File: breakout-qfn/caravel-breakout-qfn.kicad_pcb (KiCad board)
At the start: 2 copper layers, 45 x 52.5 mm, 42 parts, among them CON1 REF-182665-01, CON2 REF-182665-01, CON3 73251-1352, U1 Caravel_QFN, U2 TLV73318PDBV

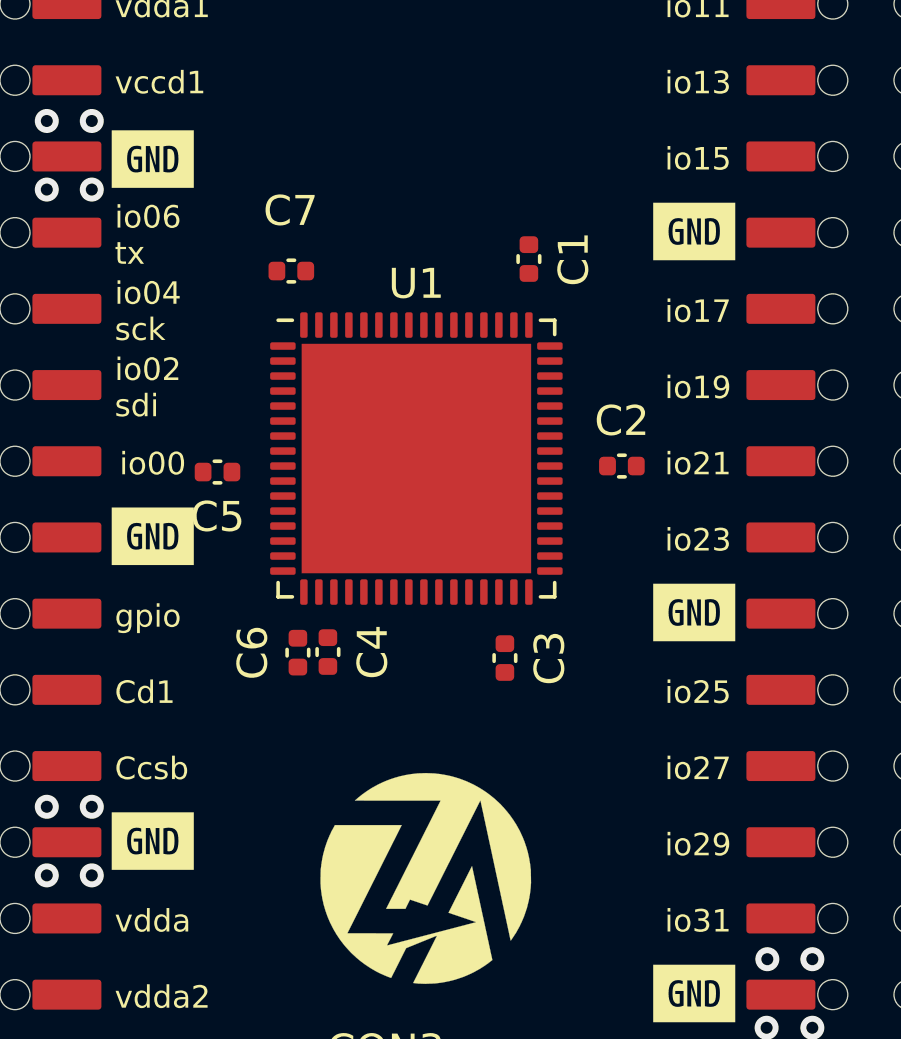
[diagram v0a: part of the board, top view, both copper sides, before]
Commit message: pre-route, DRC setup, floorplan for 2-layer top
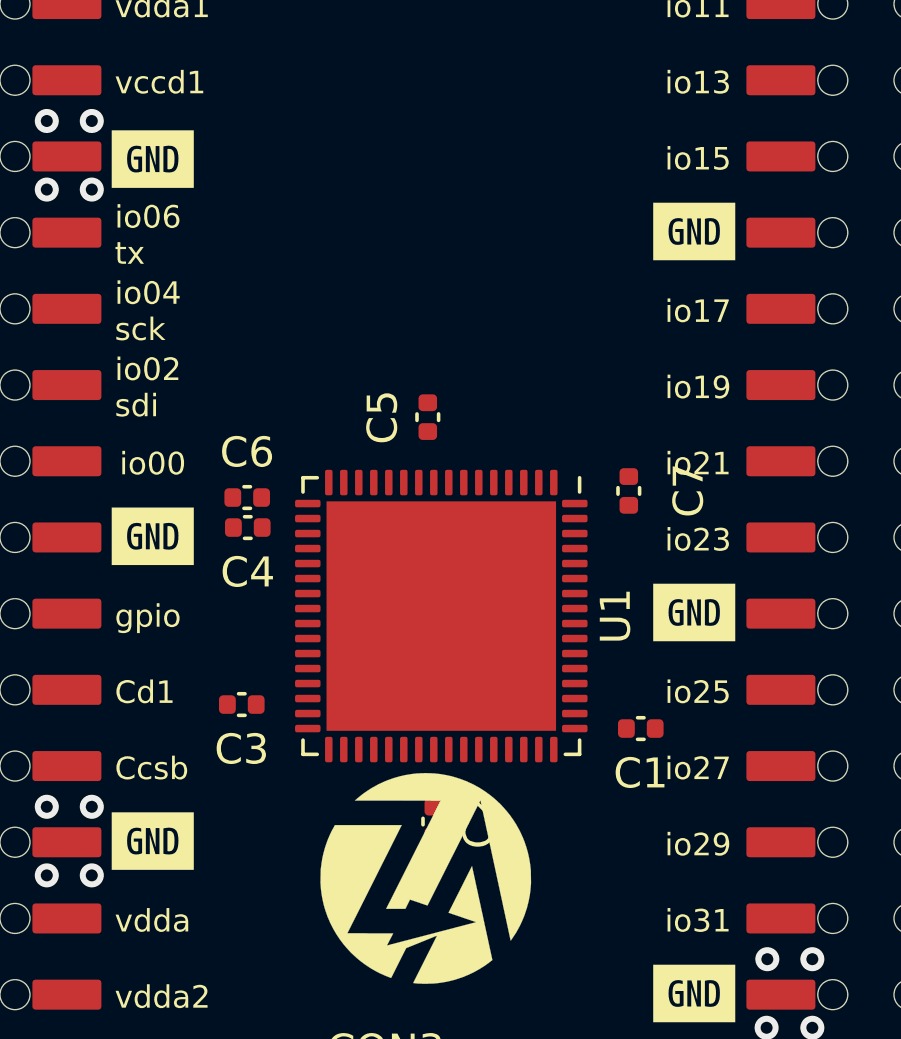
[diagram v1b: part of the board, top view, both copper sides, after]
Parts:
- moved C1 16.1 mm to (29.7, -21.1), turned to 180 degrees
- moved C7 13.4 mm to (29.3, -29.1), turned to -90 degrees
- moved C2 13.4 mm to (22.8, -18.1), turned to -90 degrees
- moved C3 8.91 mm to (16.4, -21.9), turned to 180 degrees
- moved C5 7.24 mm to (22.6, -31.5), turned to -90 degrees
- moved C6 5.44 mm to (16.6, -28.9), turned to 0 degrees
- moved U1 5.32 mm to (23.1, -24.9), turned to -90 degrees
- moved C4 4.93 mm to (16.6, -27.9), turned to 0 degrees

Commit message: routing prelim complete
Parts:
- removed C8, C9: 0.1uf, Capacitor_SMD:C_0603_1608Metric
- removed U2: TLV73318PDBV, Package_TO_SOT_SMD:SOT-23-5
- added C10: 0.1uf, Capacitor_SMD:C_0402_1005Metric, F.Cu at (28.0, -18.0)
- added C11: 0.1uf, Capacitor_SMD:C_0402_1005Metric, F.Cu at (29.3, -29.7)
- added REF**: StitchingVia-0.3mm, flyingcarsfootprints:StitchingVia-0.3mm, F.Cu at (42.5, -15.2)
- added REF**: StitchingVia-0.3mm, flyingcarsfootprints:StitchingVia-0.3mm, F.Cu at (15.0, -33.0)
- added REF**: StitchingVia-0.3mm, flyingcarsfootprints:StitchingVia-0.3mm, F.Cu at (15.0, -37.0)
- added REF**: StitchingVia-0.3mm, flyingcarsfootprints:StitchingVia-0.3mm, F.Cu at (1.80, -0.95)
- added REF**: StitchingVia-0.3mm, flyingcarsfootprints:StitchingVia-0.3mm, F.Cu at (37.4, -8.90)
- added REF**: StitchingVia-0.3mm, flyingcarsfootprints:StitchingVia-0.3mm, F.Cu at (16.9, -13.8)
- added REF**: StitchingVia-0.3mm, flyingcarsfootprints:StitchingVia-0.3mm, F.Cu at (15.0, -44.0)
- added REF**: StitchingVia-0.3mm, flyingcarsfootprints:StitchingVia-0.3mm, F.Cu at (19.6, -15.1)
- added REF**: StitchingVia-0.3mm, flyingcarsfootprints:StitchingVia-0.3mm, F.Cu at (41.3, -31.4)
- added REF**: StitchingVia-0.3mm, flyingcarsfootprints:StitchingVia-0.3mm, F.Cu at (39.3, -18.6)
- added REF**: StitchingVia-0.3mm, flyingcarsfootprints:StitchingVia-0.3mm, F.Cu at (42.5, -41.8)
- added REF**: StitchingVia-0.3mm, flyingcarsfootprints:StitchingVia-0.3mm, F.Cu at (42.5, -46.4)
- added REF**: StitchingVia-0.3mm, flyingcarsfootprints:StitchingVia-0.3mm, F.Cu at (16.9, -10.6)
- added REF**: StitchingVia-0.3mm, flyingcarsfootprints:StitchingVia-0.3mm, F.Cu at (0.70, -33.5)
- added REF**: StitchingVia-0.3mm, flyingcarsfootprints:StitchingVia-0.3mm, F.Cu at (15.0, -47.0)
- added REF**: StitchingVia-0.3mm, flyingcarsfootprints:StitchingVia-0.3mm, F.Cu at (7.60, -33.9)
- added REF**: StitchingVia-0.3mm, flyingcarsfootprints:StitchingVia-0.3mm, F.Cu at (29.4, -49.5)
- added REF**: StitchingVia-0.3mm, flyingcarsfootprints:StitchingVia-0.3mm, F.Cu at (30.0, -17.0)
- added REF**: StitchingVia-0.3mm, flyingcarsfootprints:StitchingVia-0.3mm, F.Cu at (24.8, -40.9)
- added REF**: StitchingVia-0.3mm, flyingcarsfootprints:StitchingVia-0.3mm, F.Cu at (32.4, -5.85)
- added REF**: StitchingVia-0.3mm, flyingcarsfootprints:StitchingVia-0.3mm, F.Cu at (23.7, -8.95)
- added REF**: StitchingVia-0.3mm, flyingcarsfootprints:StitchingVia-0.3mm, F.Cu at (30.0, -12.5)
- added REF**: StitchingVia-0.3mm, flyingcarsfootprints:StitchingVia-0.3mm, F.Cu at (22.1, -34.5)
- added REF**: StitchingVia-0.3mm, flyingcarsfootprints:StitchingVia-0.3mm, F.Cu at (17.9, -34.1)
- added REF**: StitchingVia-0.3mm, flyingcarsfootprints:StitchingVia-0.3mm, F.Cu at (14.8, -28.8)
- added REF**: StitchingVia-0.3mm, flyingcarsfootprints:StitchingVia-0.3mm, F.Cu at (30.0, -1.50)
- added REF**: StitchingVia-0.3mm, flyingcarsfootprints:StitchingVia-0.3mm, F.Cu at (19.9, -39.2)
- added REF**: StitchingVia-0.3mm, flyingcarsfootprints:StitchingVia-0.3mm, F.Cu at (15.0, -40.5)
- added REF**: StitchingVia-0.3mm, flyingcarsfootprints:StitchingVia-0.3mm, F.Cu at (32.8, -18.6)
- added REF**: StitchingVia-0.3mm, flyingcarsfootprints:StitchingVia-0.3mm, F.Cu at (31.7, -40.9)
- added REF**: StitchingVia-0.3mm, flyingcarsfootprints:StitchingVia-0.3mm, F.Cu at (30.0, -9.00)
- added REF**: StitchingVia-0.3mm, flyingcarsfootprints:StitchingVia-0.3mm, F.Cu at (10.6, -28.8)
- added REF**: StitchingVia-0.3mm, flyingcarsfootprints:StitchingVia-0.3mm, F.Cu at (24.4, -13.4)
- added REF**: StitchingVia-0.3mm, flyingcarsfootprints:StitchingVia-0.3mm, F.Cu at (24.8, -45.5)
- added REF**: StitchingVia-0.3mm, flyingcarsfootprints:StitchingVia-0.3mm, F.Cu at (43.1, -6.20)
- added REF**: StitchingVia-0.3mm, flyingcarsfootprints:StitchingVia-0.3mm, F.Cu at (22.8, -15.0)
- added REF**: StitchingVia-0.3mm, flyingcarsfootprints:StitchingVia-0.3mm, F.Cu at (24.8, -37.5)
- added REF**: StitchingVia-0.3mm, flyingcarsfootprints:StitchingVia-0.3mm, F.Cu at (16.9, -50.4)
- moved CON3 1.80 mm to (22.5, -4.20)
- moved C7 1.07 mm to (30.4, -29.1)
- moved C2 1.05 mm to (22.1, -18.8), turned to 180 degrees
- moved C5 0.33 mm to (22.6, -31.2), turned to 0 degrees
- moved C1 0.25 mm to (29.7, -20.9)
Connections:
- U1 pad 47: unconnected-(U1-vdda1-Pad47) -> vdda1
- U1 pad 52: unconnected-(U1-vssa1-Pad52) -> GND
- U1 pad 64: unconnected-(U1-vddio-Pad64) -> vddio
- U1 pad 65: unconnected-(U1-ThermalPad-Pad65) -> GND
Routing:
- net mprj_io[36]: track 0.00 -> 96.5 mm, vias 0 -> 6
- net mprj_io[37]: track 0.00 -> 87.1 mm, vias 0 -> 4
- net GND: track 0.00 -> 82.1 mm, vias 73 -> 86
- net mprj_io[35]: track 0.00 -> 79.3 mm, vias 0 -> 4
- net mprj_io[34]: track 0.00 -> 69.9 mm, vias 0 -> 4
- net vddio: track 0.00 -> 63.5 mm, vias 0 -> 4
- net mprj_io[8]: track 0.00 -> 62.7 mm, vias 0 -> 4
- net mprj_io[10]: track 0.00 -> 57.4 mm, vias 0 -> 4
- net vdda1: track 0.00 -> 52.9 mm, vias 0 -> 2
- net mprj_io[7]: track 0.00 -> 52.2 mm, vias 0 -> 4
- net vccd1: track 0.00 -> 47.6 mm, vias 0 -> 2
- net mprj_io[32]: track 0.00 -> 47.1 mm, vias 0 -> 2
- net mprj_io[33]: track 0.00 -> 44.9 mm, vias 0 -> 2
- net mprj_io[28]: track 0.00 -> 42.3 mm, vias 0 -> 4
- net vccd2: track 0.00 -> 42.0 mm, vias 0 -> 2
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- added copper zone on B.Cu, net GND
- added copper zone on F.Cu, net GND

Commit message: sheet and origin cleanup
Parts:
- moved C1 84.9 mm to (77.7, 49.1)
- moved C10 84.9 mm to (76.0, 52.0)
- moved C11 84.9 mm to (77.3, 40.3)
- moved C2 84.9 mm to (70.1, 51.2)
- moved C3 84.9 mm to (64.4, 48.0)
- moved C4 84.9 mm to (64.6, 42.1)
- moved C5 84.9 mm to (70.6, 38.8)
- moved C6 84.9 mm to (64.6, 41.1)
- moved C7 84.9 mm to (78.4, 40.9)
- moved CON1 84.9 mm to (55.6, 43.8)
- moved CON2 84.9 mm to (85.4, 43.8)
- moved CON3 84.9 mm to (70.5, 65.8)
- moved REF** 84.9 mm to (90.5, 54.8)
- moved REF** 84.9 mm to (63.0, 37.0)
- moved REF** 84.9 mm to (63.0, 33.0)
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
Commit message: v2.0
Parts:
- added REF**: aisler_logo_10, Logos:aisler_logo_10, F.Cu at (70.5, 26.4)
- added REF**: Logo, Logos:ef_logo, F.Cu at (70.5, 36.1)
- added REF**: Logo, Logos:ef_logo_graphical, F.Cu at (70.5, 32.1)
- added REF**: TT_logo, Logos:TT_logo, F.Cu at (70.5, 57.2)
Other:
- board text added: "Caravel QFN bkout"
- board text added: "aisler.net"
- board text added: "tinytapeout.com"
- board text added: "v2.0"
- board text removed: "ok'22"

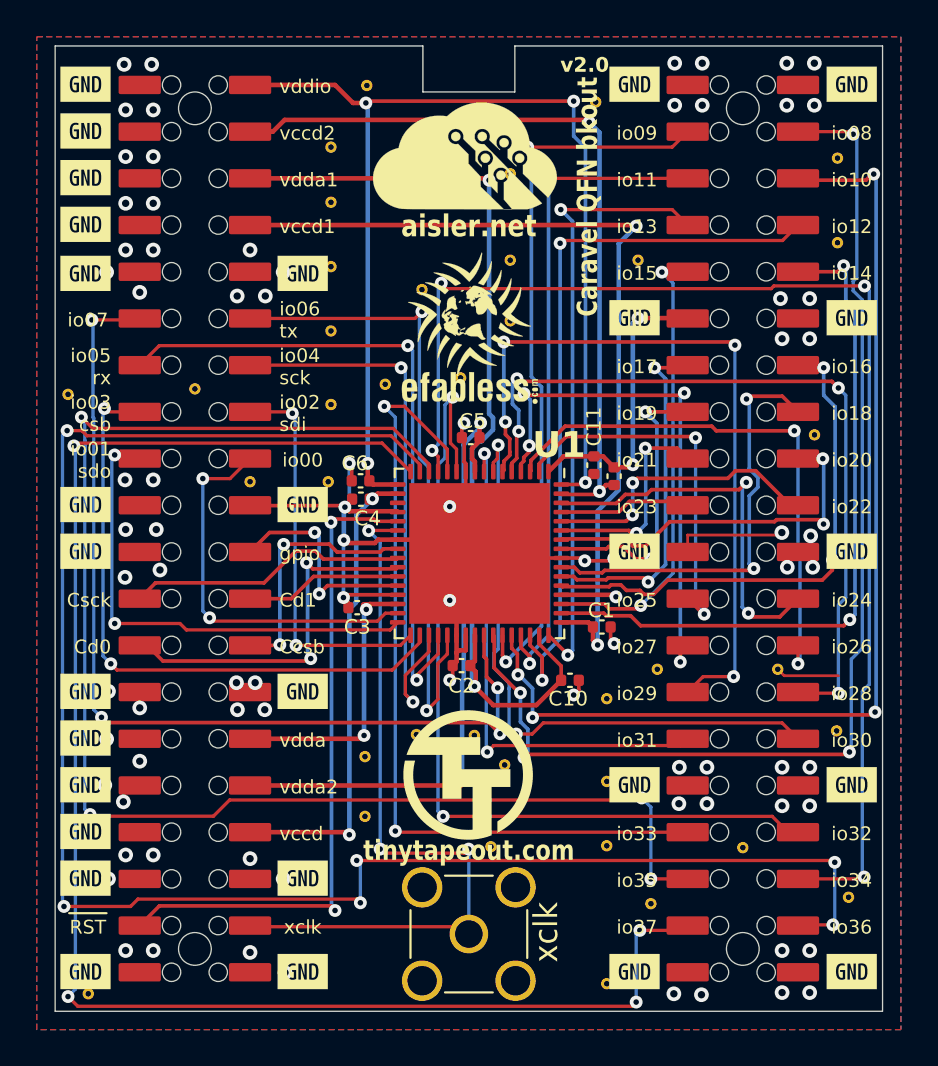
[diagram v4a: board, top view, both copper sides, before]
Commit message: QFN breakout v2.1: fixes to footprint s.masks, cleanup, flipped logos
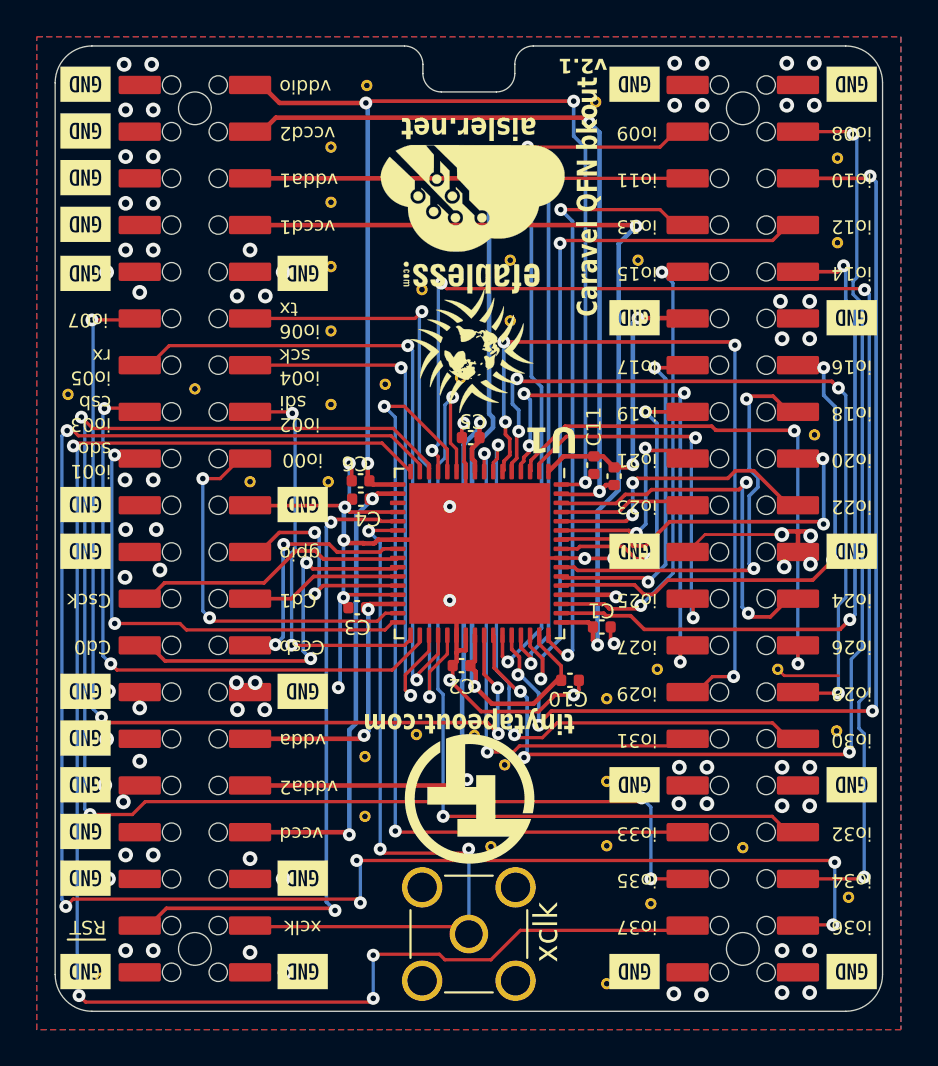
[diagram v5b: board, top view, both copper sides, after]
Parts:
- CON1, CON2: footprint ok-connectors:REF-182665-01 -> BreakoutCommon:REF-182665-01
- moved REF** 6.00 mm to (70.7, 30.1), turned to 180 degrees
- moved REF** 3.47 mm to (70.5, 22.9), turned to 180 degrees
- moved REF** 2.01 mm to (70.7, 34.1), turned to 180 degrees
- moved REF** 1.20 mm to (70.5, 58.4), turned to 180 degrees
- moved REF** 1.10 mm to (50.5, 68.2)
- turned kibuzzard-6288F08E to 180 degrees (x10)
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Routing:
- net GND: track 82.1 -> 97.1 mm, vias 86 -> 87
- net mprj_io[6]_ser_tx: track 36.1 -> 34.5 mm
- net mprj_io[37]: track 87.1 -> 85.7 mm
- net mprj_io[4]_SCK: track 31.0 -> 30.2 mm
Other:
- outline, holes or cut-outs redrawn
- board text added: "v2.1"
- board text removed: "v2.0"

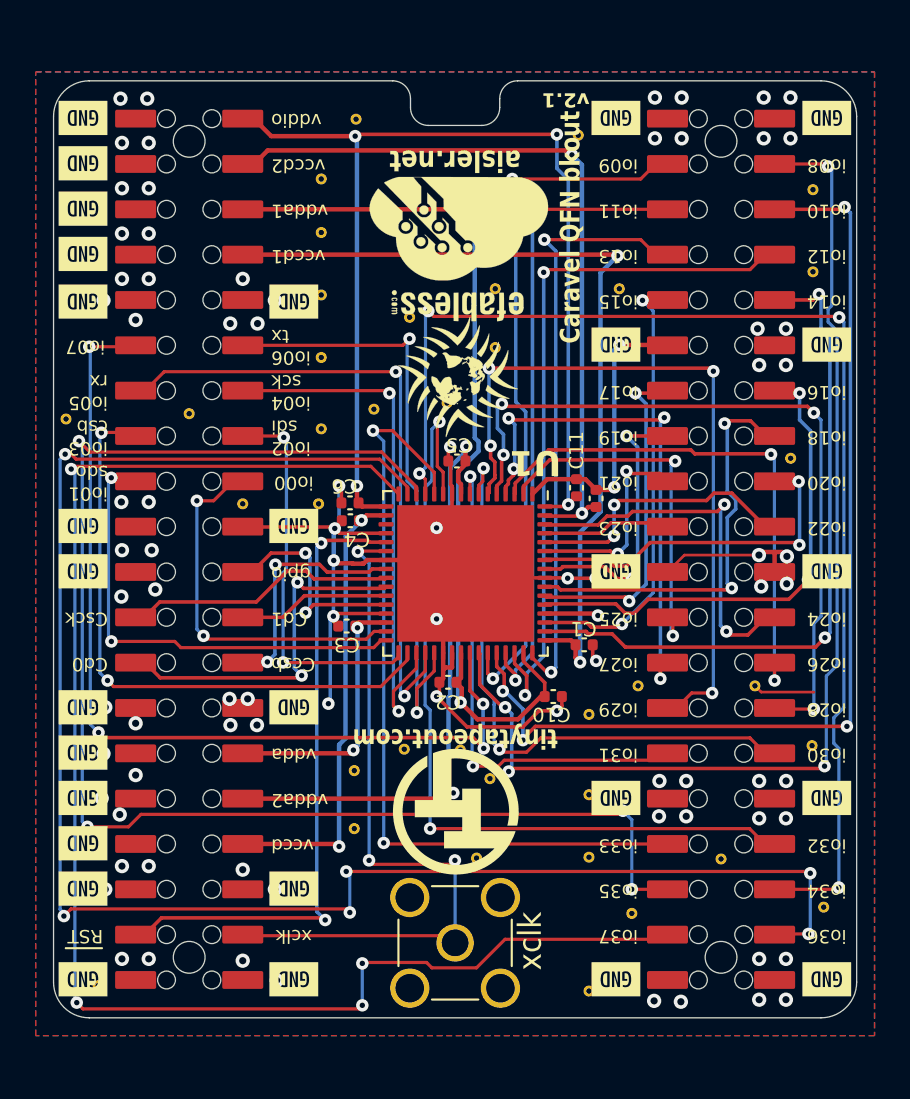
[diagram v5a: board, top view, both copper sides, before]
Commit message: QFN v2.2, using cheaper FH-00339 headers
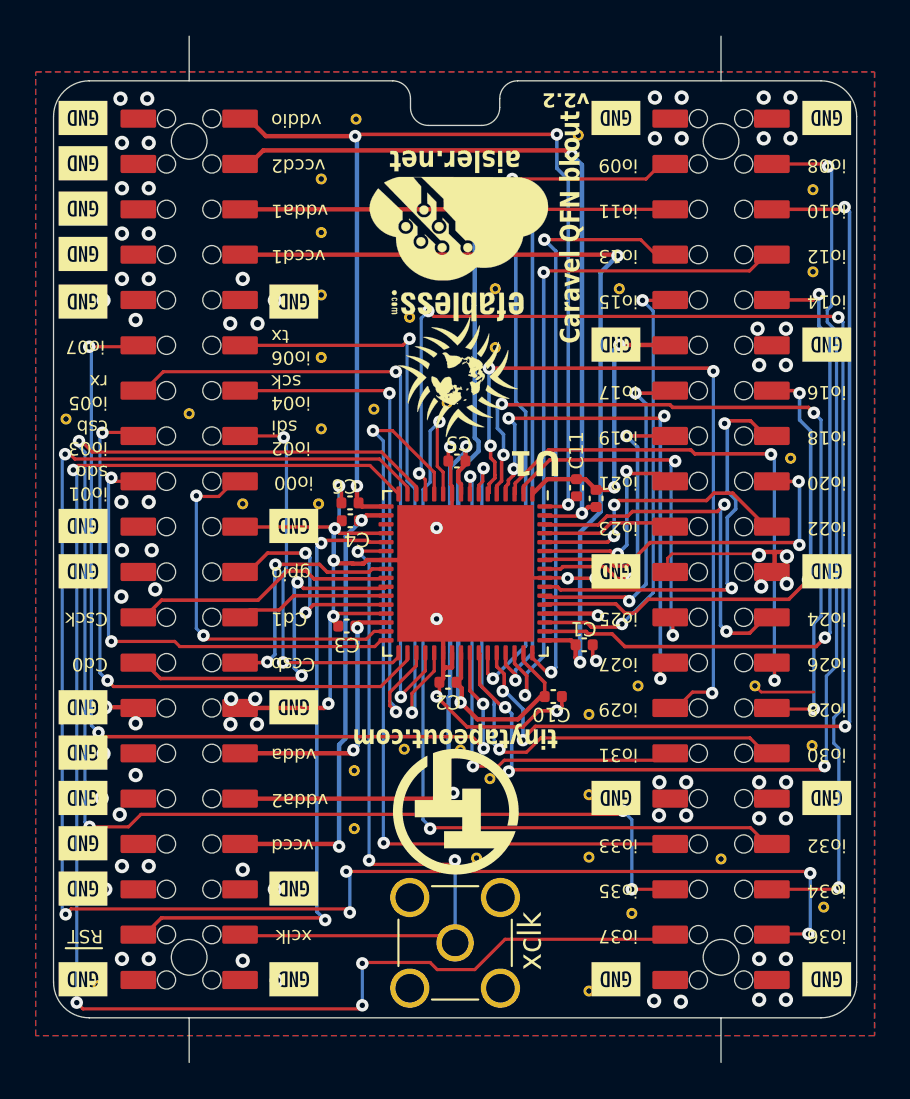
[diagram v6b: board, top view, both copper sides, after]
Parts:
- CON1, CON2: value REF-182665-01 -> FH-00339; footprint BreakoutCommon:REF-182665-01 -> BreakoutCommon:FH-00339
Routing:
- net GND: track 97.1 -> 104.5 mm
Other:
- board size 45 x 52.5 mm -> 45 x 57.5 mm
- board text added: "Bridge markers |x4"
- board text added: "v2.2"
- board text removed: "v2.1"
